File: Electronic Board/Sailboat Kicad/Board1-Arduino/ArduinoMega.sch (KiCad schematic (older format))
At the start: 7 parts, among them J2 Conn_01x08, J3 Conn_01x08, J4 Conn_01x08, J5 Conn_02x18_Odd_Even, J6 Conn_01x08, J7 Conn_01x08, J8 Conn_01x08

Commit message: Finished board-v0.1
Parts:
- added R2, R3: 4k7, Resistors_THT:R_Axial_DIN0204_L3.6mm_D1.6mm_P7.62mm_Horizontal, symbol R
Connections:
- net 20-SDA: now also R2.1
- net 21-SCL: now also R3.1
- new net 5V_Sensors: R2.2, R3.2
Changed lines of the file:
@@
 NoConn ~ 6200 2900
 NoConn ~ 6200 2800
+$Comp
+L R R3
+U 1 1 5AB57136
+P 9500 5600
+F 0 "R3" V 9580 5600 50  0000 C CNN
+F 1 "4k7" V 9500 5600 50  0000 C CNN
+F 2 "Resistors_THT:R_Axial_DIN0204_L3.6mm_D1.6mm_P7.62mm_Horizontal" V 9430 5600 50  0001 C CNN
+F 3 "" H 9500 5600 50  0001 C CNN
+	1    9500 5600
+	1    0    0    -1
+$EndComp
+$Comp
+L R R2
+U 1 1 5AB57198
+P 9400 5650
+F 0 "R2" V 9480 5650 50  0000 C CNN
+F 1 "4k7" V 9400 5650 50  0000 C CNN
+F 2 "Resistors_THT:R_Axial_DIN0204_L3.6mm_D1.6mm_P7.62mm_Horizontal" V 9330 5650 50  0001 C CNN
+F 3 "" H 9400 5650 50  0001 C CNN
+	1    9400 5650
+	1    0    0    -1
+$EndComp
+Text HLabel 9500 5950 2    60   BiDi ~ 0
+5V_Sensors
+Wire Wire Line
+	9500 5750 9500 5950
+Wire Wire Line
+	9400 5800 9400 5950
+Wire Wire Line
+	9400 5950 9500 5950
+Wire Wire Line
+	9500 5450 9500 5250
+Wire Wire Line
+	9400 5500 9400 5150
 $EndSCHEMATC

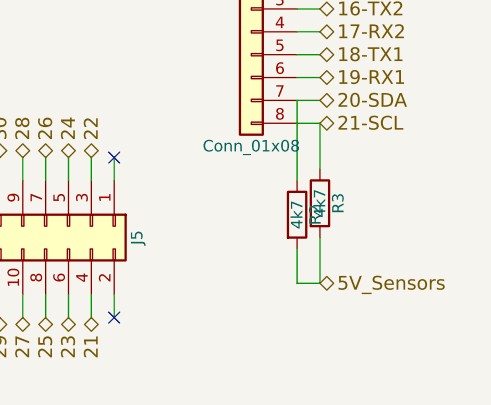
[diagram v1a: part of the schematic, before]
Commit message: Cleaned up, and added security, text and better usability, preparation for board v2
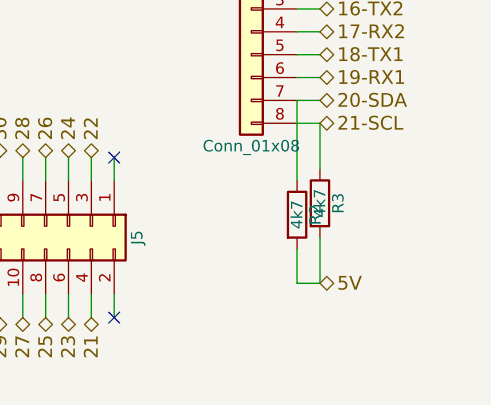
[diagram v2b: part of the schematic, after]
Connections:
- net 5V_Sensors is gone; now on net 5V: R2.2, R3.2
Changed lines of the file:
@@
 	1    0    0    -1
 $EndComp
-Text HLabel 9500 5950 2    60   BiDi ~ 0
-5V_Sensors
 Wire Wire Line
 	9500 5750 9500 5950
@@
 Wire Wire Line
 	9400 5500 9400 5150
+Text HLabel 9500 5950 2    60   BiDi ~ 0
+5V
 $EndSCHEMATC

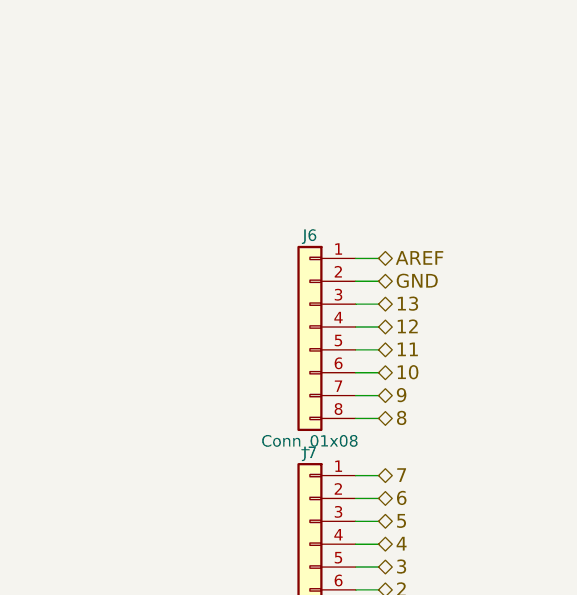
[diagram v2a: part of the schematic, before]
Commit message: added decoupler capacitor for voltage measurements and added connectors to arduino
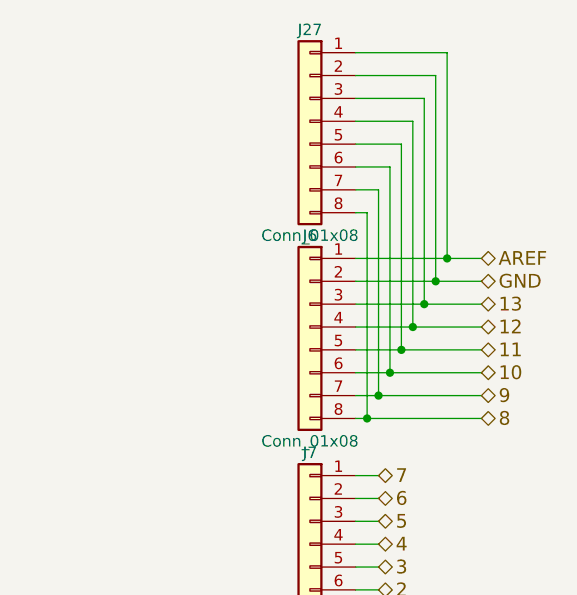
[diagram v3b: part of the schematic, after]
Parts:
- added J27: Conn_01x08, Pin_Headers:Pin_Header_Straight_1x08_Pitch2.54mm, symbol Conn_01x08
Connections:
- net 10: now also J27.6 (Pin_6)
- net 11: now also J27.5 (Pin_5)
- net 12: now also J27.4 (Pin_4)
- net 13: now also J27.3 (Pin_3)
- net 8: now also J27.8 (Pin_8)
- net 9: now also J27.7 (Pin_7)
- net AREF: now also J27.1 (Pin_1)
- net GND: now also J27.2 (Pin_2)
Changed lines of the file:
@@
 	1    0    0    -1
 $EndComp
-Text HLabel 9500 2650 2    60   BiDi ~ 0
+Text HLabel 9950 2650 2    60   BiDi ~ 0
 AREF
-Text HLabel 9500 2750 2    60   BiDi ~ 0
+Text HLabel 9950 2750 2    60   BiDi ~ 0
 GND
-Text HLabel 9500 2850 2    60   BiDi ~ 0
+Text HLabel 9950 2850 2    60   BiDi ~ 0
 13
-Text HLabel 9500 2950 2    60   BiDi ~ 0
+Text HLabel 9950 2950 2    60   BiDi ~ 0
 12
-Text HLabel 9500 3050 2    60   BiDi ~ 0
+Text HLabel 9950 3050 2    60   BiDi ~ 0
 11
-Text HLabel 9500 3150 2    60   BiDi ~ 0
+Text HLabel 9950 3150 2    60   BiDi ~ 0
 10
-Text HLabel 9500 3250 2    60   BiDi ~ 0
+Text HLabel 9950 3250 2    60   BiDi ~ 0
 9
-Text HLabel 9500 3350 2    60   BiDi ~ 0
+Text HLabel 9950 3350 2    60   BiDi ~ 0
 8
 Text HLabel 9500 3600 2    60   BiDi ~ 0
@@
 Text HLabel 9500 5250 2    60   BiDi ~ 0
 21-SCL
-Wire Wire Line
-	9400 2650 9500 2650
-Wire Wire Line
-	9500 2750 9400 2750
-Wire Wire Line
-	9400 2850 9500 2850
-Wire Wire Line
-	9500 2950 9400 2950
-Wire Wire Line
-	9400 3050 9500 3050
-Wire Wire Line
-	9500 3150 9400 3150
-Wire Wire Line
-	9400 3250 9500 3250
-Wire Wire Line
-	9500 3350 9400 3350
 Wire Wire Line
 	9400 3600 9500 3600
@@
 Text HLabel 9500 5950 2    60   BiDi ~ 0
 5V
+$Comp
+L Conn_01x08 J27
+U 1 1 5B9ADC25
+P 9200 2050
+F 0 "J27" H 9200 2450 50  0000 C CNN
+F 1 "Conn_01x08" H 9200 1550 50  0000 C CNN
+F 2 "Pin_Headers:Pin_Header_Straight_1x08_Pitch2.54mm" H 9200 2050 50  0001 C CNN
+F 3 "" H 9200 2050 50  0001 C CNN
+	1    9200 2050
+	-1   0    0    -1
+$EndComp
+Wire Wire Line
+	9400 3350 9950 3350
+Wire Wire Line
+	9450 3350 9450 2450
+Wire Wire Line
+	9450 2450 9400 2450
+Wire Wire Line
+	9400 3250 9950 3250
+Wire Wire Line
+	9500 3250 9500 2350
+Wire Wire Line
+	9500 2350 9400 2350
+Wire Wire Line
+	9400 3150 9950 3150
+Wire Wire Line
+	9550 3150 9550 2250
+Wire Wire Line
+	9550 2250 9400 2250
+Wire Wire Line
+	9400 3050 9950 3050
+Wire Wire Line
+	9600 3050 9600 2150
+Wire Wire Line
+	9600 2150 9400 2150
+Wire Wire Line
+	9400 2950 9950 2950
+Wire Wire Line
+	9650 2950 9650 2050
+Wire Wire Line
+	9650 2050 9400 2050
+Wire Wire Line
+	9400 2850 9950 2850
+Wire Wire Line
+	9700 2850 9700 1950
+Wire Wire Line
+	9700 1950 9400 1950
+Wire Wire Line
+	9400 2750 9950 2750
+Wire Wire Line
+	9750 2750 9750 1850
+Wire Wire Line
+	9750 1850 9400 1850
+Wire Wire Line
+	9400 2650 9950 2650
+Wire Wire Line
+	9800 2650 9800 1750
+Wire Wire Line
+	9800 1750 9400 1750
+Connection ~ 9800 2650
+Connection ~ 9750 2750
+Connection ~ 9700 2850
+Connection ~ 9650 2950
+Connection ~ 9600 3050
+Connection ~ 9550 3150
+Connection ~ 9500 3250
+Connection ~ 9450 3350
 $EndSCHEMATC

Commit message: Updated version of Kicad, rendered images and BOM
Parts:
- removed J2, J27, J3, J4, J6, J7, J8: Conn_01x08, Pin_Headers:Pin_Header_Straight_1x08_Pitch2.54mm, symbol Conn_01x08
- removed J5: Conn_02x18_Odd_Even, Pin_Headers:Pin_Header_Straight_2x18_Pitch2.54mm, symbol Conn_02x18_Odd_Even
- added J26, J27, J28, J30, J31, J32, J33: Conn_01x08_Male, Connector_PinHeader_2.54mm:PinHeader_1x08_P2.54mm_Vertical, symbol Connector:Conn_01x08_Male
- added J29: Conn_02x18_Odd_Even, Connector_PinHeader_2.54mm:PinHeader_2x18_P2.54mm_Vertical, symbol Connector_Generic:Conn_02x18_Odd_Even
- R2, R3: footprint Resistors_THT:R_Axial_DIN0204_L3.6mm_D1.6mm_P7.62mm_Horizontal -> Resistor_THT:R_Axial_DIN0204_L3.6mm_D1.6mm_P7.62mm_Horizontal; symbol R -> Device:R
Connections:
- net 0: now also J32.8 (Pin_8)
- net 1: now also J32.7 (Pin_7)
- net 10: now also J30.6 (Pin_6), J31.6 (Pin_6)
- net 11: now also J30.5 (Pin_5), J31.5 (Pin_5)
- net 12: now also J30.4 (Pin_4), J31.4 (Pin_4)
- net 13: now also J30.3 (Pin_3), J31.3 (Pin_3)
- net 14-TX3: now also J33.1 (Pin_1)
- net 15-RX3: now also J33.2 (Pin_2)
- net 16-TX2: now also J33.3 (Pin_3)
- net 17-RX2: now also J33.4 (Pin_4)
- net 18-TX1: now also J33.5 (Pin_5)
- net 19-RX1: now also J33.6 (Pin_6)
- net 2: now also J32.6 (Pin_6)
- net 20-SDA: now also J33.7 (Pin_7)
- net 21: now also J29.4 (Pin_4)
- net 21-SCL: now also J33.8 (Pin_8)
- net 22: now also J29.3 (Pin_3)
- net 23: now also J29.6 (Pin_6)
- net 24: now also J29.5 (Pin_5)
- net 25: now also J29.8 (Pin_8)
- net 26: now also J29.7 (Pin_7)
- net 27: now also J29.10 (Pin_10)
- net 28: now also J29.9 (Pin_9)
- net 29: now also J29.12 (Pin_12)
- net 3: now also J32.5 (Pin_5)
- net 3.3V: now also J26.4 (Pin_4)
- net 30: now also J29.11 (Pin_11)
- net 31: now also J29.14 (Pin_14)
- net 32: now also J29.13 (Pin_13)
- net 33: now also J29.16 (Pin_16)
- net 34: now also J29.15 (Pin_15)
- net 35: now also J29.18 (Pin_18)
- net 36: now also J29.17 (Pin_17)
- net 37: now also J29.20 (Pin_20)
- net 38: now also J29.19 (Pin_19)
- net 39: now also J29.22 (Pin_22)
- net 4: now also J32.4 (Pin_4)
- net 40: now also J29.21 (Pin_21)
- net 41: now also J29.24 (Pin_24)
- net 42: now also J29.23 (Pin_23)
- net 43: now also J29.26 (Pin_26)
- net 44: now also J29.25 (Pin_25)
- net 45: now also J29.28 (Pin_28)
- net 46: now also J29.27 (Pin_27)
- net 47: now also J29.30 (Pin_30)
- net 48: now also J29.29 (Pin_29)
- net 5: now also J32.3 (Pin_3)
- net 50: now also J29.31 (Pin_31)
- net 51: now also J29.32 (Pin_32)
- net 52: now also J29.33 (Pin_33)
- net 53: now also J29.34 (Pin_34)
- net 5V: now also J26.5 (Pin_5)
- net 6: now also J32.2 (Pin_2)
- net 7: now also J32.1 (Pin_1)
- net 8: now also J30.8 (Pin_8), J31.8 (Pin_8)
- net 9: now also J30.7 (Pin_7), J31.7 (Pin_7)
- net A0: now also J27.1 (Pin_1)
- net A1: now also J27.2 (Pin_2)
- net A10: now also J28.3 (Pin_3)
- net A11: now also J28.4 (Pin_4)
- net A12: now also J28.5 (Pin_5)
- net A13: now also J28.6 (Pin_6)
- net A14: now also J28.7 (Pin_7)
- net A15: now also J28.8 (Pin_8)
- net A2: now also J27.3 (Pin_3)
- net A3: now also J27.4 (Pin_4)
- net A4: now also J27.5 (Pin_5)
- net A5: now also J27.6 (Pin_6)
- net A6: now also J27.7 (Pin_7)
- net A7: now also J27.8 (Pin_8)
- net A8: now also J28.1 (Pin_1)
- net A9: now also J28.2 (Pin_2)
- net AREF: now also J30.1 (Pin_1), J31.1 (Pin_1)
- net GND: now also J26.6 (Pin_6), J26.7 (Pin_7), J29.35 (Pin_35), J29.36 (Pin_36), J30.2 (Pin_2), J31.2 (Pin_2)
- net RESET: now also J26.3 (Pin_3)
- net Vin: now also J26.8 (Pin_8)
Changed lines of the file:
@@
-EESchema Schematic File Version 2
-LIBS:power
-LIBS:device
-LIBS:switches
-LIBS:relays
-LIBS:motors
-LIBS:transistors
-LIBS:conn
-LIBS:linear
-LIBS:regul
-LIBS:74xx
-LIBS:cmos4000
-LIBS:adc-dac
-LIBS:memory
-LIBS:xilinx
-LIBS:microcontrollers
-LIBS:dsp
-LIBS:microchip
-LIBS:analog_switches
-LIBS:motorola
-LIBS:texas
-LIBS:intel
-LIBS:audio
-LIBS:interface
-LIBS:digital-audio
-LIBS:philips
-LIBS:display
-LIBS:cypress
-LIBS:siliconi
-LIBS:opto
-LIBS:atmel
-LIBS:contrib
-LIBS:valves
+EESchema Schematic File Version 4
 LIBS:Arduino Interface-cache
-EELAYER 25 0
+EELAYER 26 0
 EELAYER END
 $Descr A4 11693 8268
@@
 Comment4 ""
 $EndDescr
-$Comp
-L Conn_01x08 J6
-U 1 1 5A0CB4F8
-P 9200 2950
-F 0 "J6" H 9200 3350 50  0000 C CNN
-F 1 "Conn_01x08" H 9200 2450 50  0000 C CNN
-F 2 "Pin_Headers:Pin_Header_Straight_1x08_Pitch2.54mm" H 9200 2950 50  0001 C CNN
-F 3 "" H 9200 2950 50  0001 C CNN
-	1    9200 2950
-	-1   0    0    -1
-$EndComp
-$Comp
-L Conn_01x08 J7
-U 1 1 5A0CB552
-P 9200 3900
-F 0 "J7" H 9200 4300 50  0000 C CNN
-F 1 "Conn_01x08" H 9200 3400 50  0000 C CNN
-F 2 "Pin_Headers:Pin_Header_Straight_1x08_Pitch2.54mm" H 9200 3900 50  0001 C CNN
-F 3 "" H 9200 3900 50  0001 C CNN
-	1    9200 3900
-	-1   0    0    -1
-$EndComp
-$Comp
-L Conn_01x08 J8
-U 1 1 5A0CB57C
-P 9200 4850
-F 0 "J8" H 9200 5250 50  0000 C CNN
-F 1 "Conn_01x08" H 9200 4350 50  0000 C CNN
-F 2 "Pin_Headers:Pin_Header_Straight_1x08_Pitch2.54mm" H 9200 4850 50  0001 C CNN
-F 3 "" H 9200 4850 50  0001 C CNN
-	1    9200 4850
-	-1   0    0    -1
-$EndComp
-$Comp
-L Conn_01x08 J4
-U 1 1 5A0CB6B4
-P 6400 5050
-F 0 "J4" H 6400 5450 50  0000 C CNN
-F 1 "Conn_01x08" H 6400 4550 50  0000 C CNN
-F 2 "Pin_Headers:Pin_Header_Straight_1x08_Pitch2.54mm" H 6400 5050 50  0001 C CNN
-F 3 "" H 6400 5050 50  0001 C CNN
-	1    6400 5050
-	1    0    0    -1
-$EndComp
-$Comp
-L Conn_01x08 J3
-U 1 1 5A0CB705
-P 6400 4050
-F 0 "J3" H 6400 4450 50  0000 C CNN
-F 1 "Conn_01x08" H 6400 3550 50  0000 C CNN
-F 2 "Pin_Headers:Pin_Header_Straight_1x08_Pitch2.54mm" H 6400 4050 50  0001 C CNN
-F 3 "" H 6400 4050 50  0001 C CNN
-	1    6400 4050
-	1    0    0    -1
-$EndComp
 Text HLabel 9950 2650 2    60   BiDi ~ 0
 AREF
@@
 Text HLabel 7100 6100 3    60   BiDi ~ 0
 51
-$Comp
-L Conn_02x18_Odd_Even J5
-U 1 1 5A0CC6EF
-P 7800 5700
-F 0 "J5" H 7850 6600 50  0000 C CNN
-F 1 "Conn_02x18_Odd_Even" H 7850 4700 50  0000 C CNN
-F 2 "Pin_Headers:Pin_Header_Straight_2x18_Pitch2.54mm" H 7800 5700 50  0001 C CNN
-F 3 "" H 7800 5700 50  0001 C CNN
-	1    7800 5700
-	0    1    1    0
-$EndComp
 NoConn ~ 8600 5400
 NoConn ~ 8600 6100
-$Comp
-L Conn_01x08 J2
-U 1 1 5A997527
-P 6400 3100
-F 0 "J2" H 6400 3500 50  0000 C CNN
-F 1 "Conn_01x08" H 6400 2600 50  0000 C CNN
-F 2 "Pin_Headers:Pin_Header_Straight_1x08_Pitch2.54mm" H 6400 3100 50  0001 C CNN
-F 3 "" H 6400 3100 50  0001 C CNN
-	1    6400 3100
-	1    0    0    -1
-$EndComp
 NoConn ~ 6200 2900
 NoConn ~ 6200 2800
 $Comp
-L R R3
+L Device:R R3
 U 1 1 5AB57136
 P 9500 5600
 F 0 "R3" V 9580 5600 50  0000 C CNN
 F 1 "4k7" V 9500 5600 50  0000 C CNN
-F 2 "Resistors_THT:R_Axial_DIN0204_L3.6mm_D1.6mm_P7.62mm_Horizontal" V 9430 5600 50  0001 C CNN
+F 2 "Resistor_THT:R_Axial_DIN0204_L3.6mm_D1.6mm_P7.62mm_Horizontal" V 9430 5600 50  0001 C CNN
 F 3 "" H 9500 5600 50  0001 C CNN
 	1    9500 5600
@@
 $EndComp
 $Comp
-L R R2
+L Device:R R2
 U 1 1 5AB57198
 P 9400 5650
 F 0 "R2" V 9480 5650 50  0000 C CNN
 F 1 "4k7" V 9400 5650 50  0000 C CNN
-F 2 "Resistors_THT:R_Axial_DIN0204_L3.6mm_D1.6mm_P7.62mm_Horizontal" V 9330 5650 50  0001 C CNN
+F 2 "Resistor_THT:R_Axial_DIN0204_L3.6mm_D1.6mm_P7.62mm_Horizontal" V 9330 5650 50  0001 C CNN
 F 3 "" H 9400 5650 50  0001 C CNN
 	1    9400 5650
@@
 Wire Wire Line
 	9500 5450 9500 5250
-Wire Wire Line
-	9400 5500 9400 5150
 Text HLabel 9500 5950 2    60   BiDi ~ 0
 5V
-$Comp
-L Conn_01x08 J27
-U 1 1 5B9ADC25
-P 9200 2050
-F 0 "J27" H 9200 2450 50  0000 C CNN
-F 1 "Conn_01x08" H 9200 1550 50  0000 C CNN
-F 2 "Pin_Headers:Pin_Header_Straight_1x08_Pitch2.54mm" H 9200 2050 50  0001 C CNN
-F 3 "" H 9200 2050 50  0001 C CNN
-	1    9200 2050
-	-1   0    0    -1
-$EndComp
-Wire Wire Line
-	9400 3350 9950 3350
+Wire Wire Line
+	9400 3350 9450 3350
 Wire Wire Line
 	9450 3350 9450 2450
@@
 	9450 2450 9400 2450
 Wire Wire Line
-	9400 3250 9950 3250
+	9400 3250 9500 3250
 Wire Wire Line
 	9500 3250 9500 2350
@@
 	9500 2350 9400 2350
 Wire Wire Line
-	9400 3150 9950 3150
+	9400 3150 9550 3150
 Wire Wire Line
 	9550 3150 9550 2250
@@
 	9550 2250 9400 2250
 Wire Wire Line
-	9400 3050 9950 3050
+	9400 3050 9600 3050
 Wire Wire Line
 	9600 3050 9600 2150
@@
 	9600 2150 9400 2150
 Wire Wire Line
-	9400 2950 9950 2950
+	9400 2950 9650 2950
 Wire Wire Line
 	9650 2950 9650 2050
@@
 	9650 2050 9400 2050
 Wire Wire Line
-	9400 2850 9950 2850
+	9400 2850 9700 2850
 Wire Wire Line
 	9700 2850 9700 1950
@@
 	9700 1950 9400 1950
 Wire Wire Line
-	9400 2750 9950 2750
+	9400 2750 9750 2750
 Wire Wire Line
 	9750 2750 9750 1850
@@
 	9750 1850 9400 1850
 Wire Wire Line
-	9400 2650 9950 2650
+	9400 2650 9800 2650
 Wire Wire Line
 	9800 2650 9800 1750
@@
 Connection ~ 9500 3250
 Connection ~ 9450 3350
+Wire Wire Line
+	9800 2650 9950 2650
+Wire Wire Line
+	9750 2750 9950 2750
+Wire Wire Line
+	9700 2850 9950 2850
+Wire Wire Line
+	9650 2950 9950 2950
+Wire Wire Line
+	9600 3050 9950 3050
+Wire Wire Line
+	9550 3150 9950 3150
+Wire Wire Line
+	9500 3250 9950 3250
+Wire Wire Line
+	9450 3350 9950 3350
+$Comp
+L Connector:Conn_01x08_Male J27
+U 1 1 5CFFF8D2
+P 6400 4050
+F 0 "J27" H 6373 4023 50  0000 R CNN
+F 1 "Conn_01x08_Male" H 6373 3932 50  0000 R CNN
+F 2 "Connector_PinHeader_2.54mm:PinHeader_1x08_P2.54mm_Vertical" H 6400 4050 50  0001 C CNN
+F 3 "~" H 6400 4050 50  0001 C CNN
+	1    6400 4050
+	-1   0    0    -1
+$EndComp
+$Comp
+L Connector:Conn_01x08_Male J28
+U 1 1 5CFFFAC8
+P 6400 5050
+F 0 "J28" H 6373 5023 50  0000 R CNN
+F 1 "Conn_01x08_Male" H 6373 4932 50  0000 R CNN
+F 2 "Connector_PinHeader_2.54mm:PinHeader_1x08_P2.54mm_Vertical" H 6400 5050 50  0001 C CNN
+F 3 "~" H 6400 5050 50  0001 C CNN
+	1    6400 5050
+	-1   0    0    -1
+$EndComp
+$Comp
+L Connector:Conn_01x08_Male J32
+U 1 1 5CFFFAF0
+P 9200 3900
+F 0 "J32" H 9306 4378 50  0000 C CNN
+F 1 "Conn_01x08_Male" H 9306 4287 50  0000 C CNN
+F 2 "Connector_PinHeader_2.54mm:PinHeader_1x08_P2.54mm_Vertical" H 9200 3900 50  0001 C CNN
+F 3 "~" H 9200 3900 50  0001 C CNN
+	1    9200 3900
+	1    0    0    -1
+$EndComp
+$Comp
+L Connector:Conn_01x08_Male J33
+U 1 1 5CFFFB62
+P 9200 4850
+F 0 "J33" H 9306 5328 50  0000 C CNN
+F 1 "Conn_01x08_Male" H 9306 5237 50  0000 C CNN
+F 2 "Connector_PinHeader_2.54mm:PinHeader_1x08_P2.54mm_Vertical" H 9200 4850 50  0001 C CNN
+F 3 "~" H 9200 4850 50  0001 C CNN
+	1    9200 4850
+	1    0    0    -1
+$EndComp
+$Comp
+L Connector:Conn_01x08_Male J31
+U 1 1 5CFFFB9C
+P 9200 2950
+F 0 "J31" H 9306 3428 50  0000 C CNN
+F 1 "Conn_01x08_Male" H 9306 3337 50  0000 C CNN
+F 2 "Connector_PinHeader_2.54mm:PinHeader_1x08_P2.54mm_Vertical" H 9200 2950 50  0001 C CNN
+F 3 "~" H 9200 2950 50  0001 C CNN
+	1    9200 2950
+	1    0    0    -1
+$EndComp
+$Comp
+L Connector:Conn_01x08_Male J30
+U 1 1 5CFFFC14
+P 9200 2050
+F 0 "J30" H 9306 2528 50  0000 C CNN
+F 1 "Conn_01x08_Male" H 9306 2437 50  0000 C CNN
+F 2 "Connector_PinHeader_2.54mm:PinHeader_1x08_P2.54mm_Vertical" H 9200 2050 50  0001 C CNN
+F 3 "~" H 9200 2050 50  0001 C CNN
+	1    9200 2050
+	1    0    0    -1
+$EndComp
+$Comp
+L Connector:Conn_01x08_Male J26
+U 1 1 5CFFFD42
+P 6400 3100
+F 0 "J26" H 6373 3073 50  0000 R CNN
+F 1 "Conn_01x08_Male" H 6373 2982 50  0000 R CNN
+F 2 "Connector_PinHeader_2.54mm:PinHeader_1x08_P2.54mm_Vertical" H 6400 3100 50  0001 C CNN
+F 3 "~" H 6400 3100 50  0001 C CNN
+	1    6400 3100
+	-1   0    0    -1
+$EndComp
+$Comp
+L Connector_Generic:Conn_02x18_Odd_Even J29
+U 1 1 5D0004CB
+P 7800 5700
+F 0 "J29" V 7804 4713 50  0000 R CNN
+F 1 "Conn_02x18_Odd_Even" V 7895 4713 50  0000 R CNN
+F 2 "Connector_PinHeader_2.54mm:PinHeader_2x18_P2.54mm_Vertical" H 7800 5700 50  0001 C CNN
+F 3 "~" H 7800 5700 50  0001 C CNN
+	1    7800 5700
+	0    1    1    0
+$EndComp
+Connection ~ 9400 5150
+Wire Wire Line
+	9400 5150 9400 5500
 $EndSCHEMATC
